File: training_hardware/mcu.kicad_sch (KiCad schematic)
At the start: 2 parts, among them J1 RJ45_LED_Shielded, U1 Teensy4.1_DEV-16771

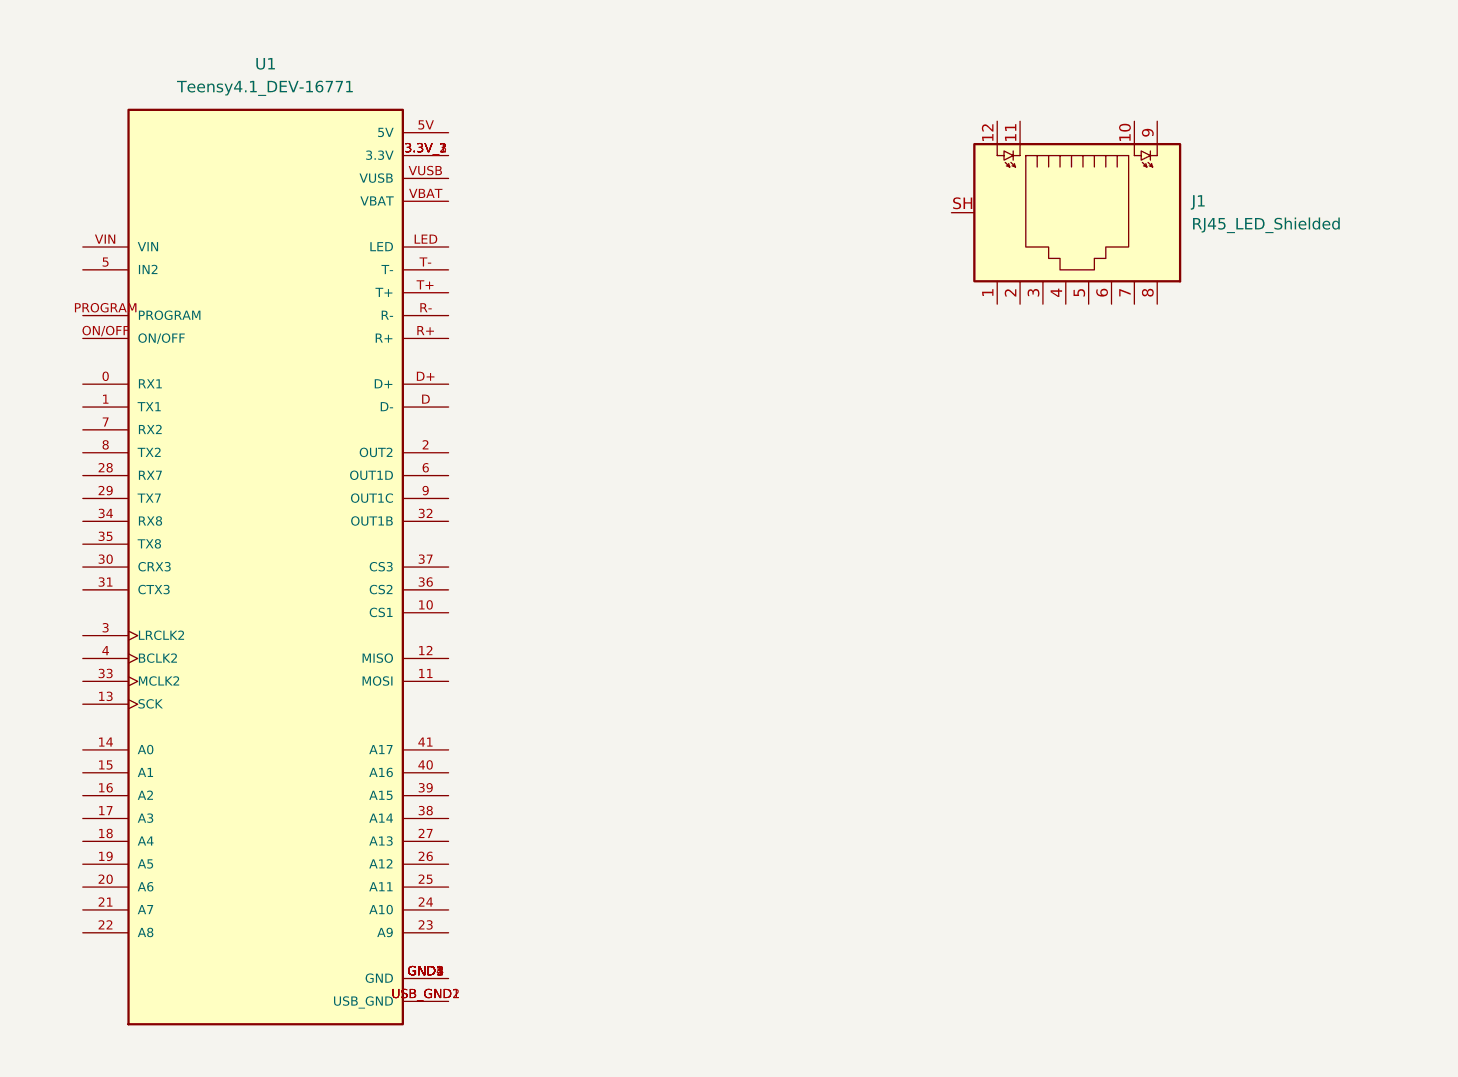
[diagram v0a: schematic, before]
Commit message: Add Ethernet
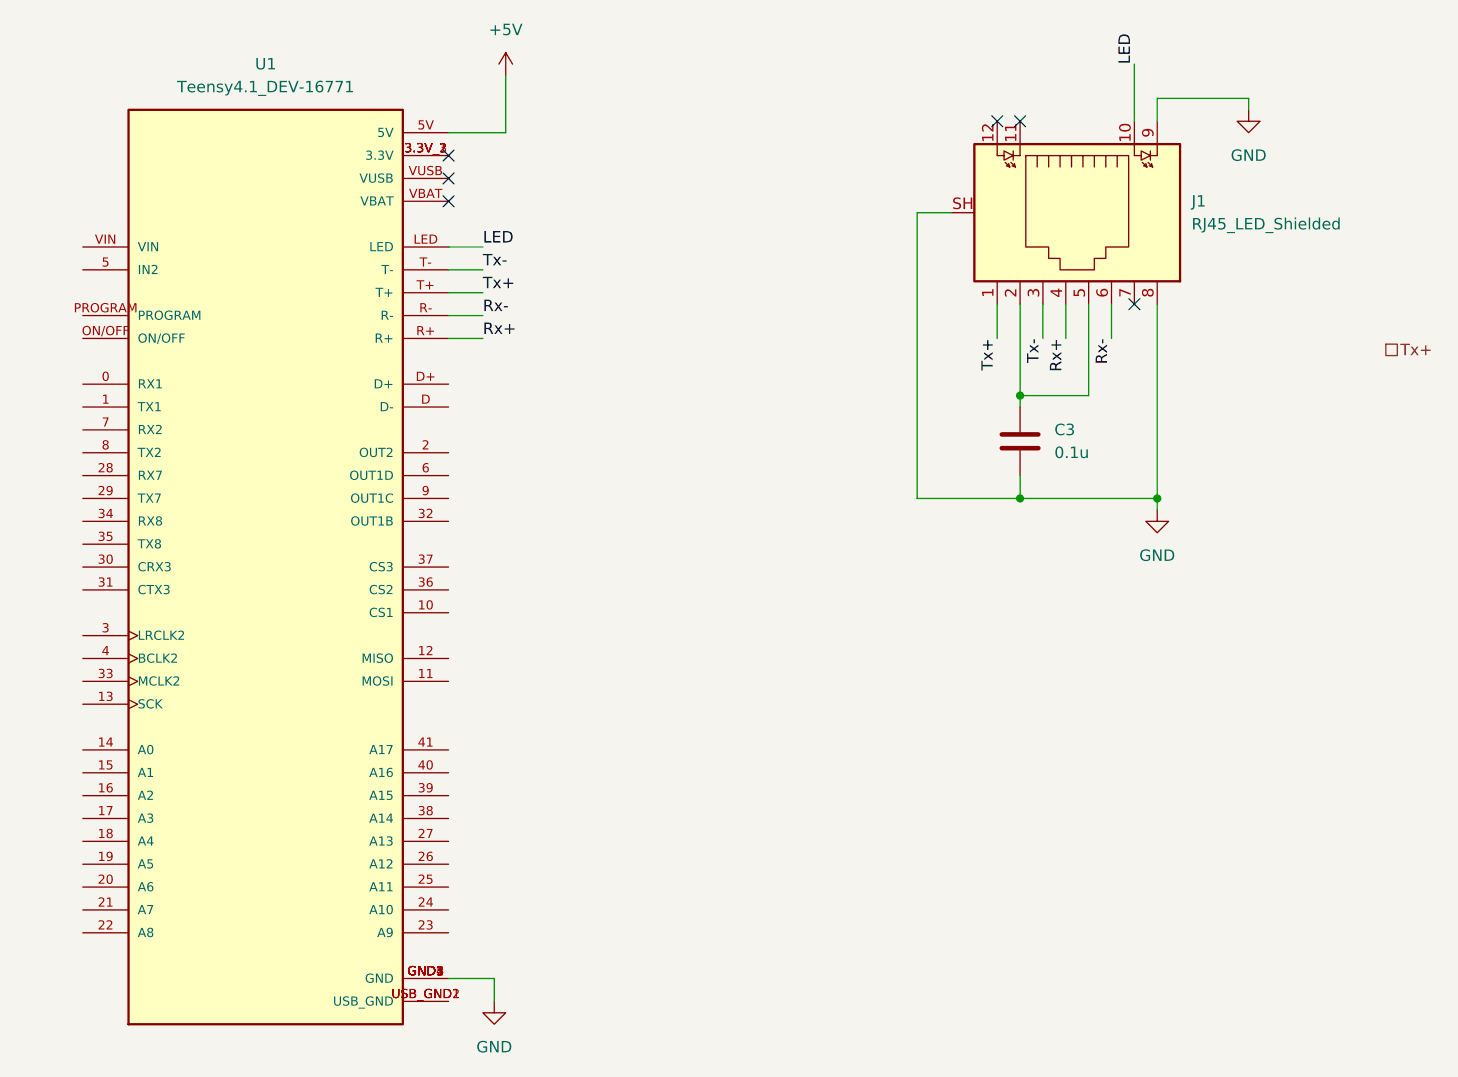
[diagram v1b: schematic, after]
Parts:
- added C3: 0.1u, symbol Device:C
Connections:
- net Tx+: now reaches J1.1
- net Tx+: now also U1.T+
- net LED: now reaches J1.10
- net LED: now also U1.LED
- net at J1.2: now also J1.5, C3.1
- net Tx-: now reaches J1.3
- net Tx-: now also U1.T-
- net Rx+: now reaches J1.4
- net Rx+: now also U1.R+
- net Rx-: now reaches J1.6
- net Rx-: now also U1.R-
- net GND: now reaches J1.8
- net GND: now also J1.9, J1.SH, U1.GND1 (GND), U1.GND2 (GND), U1.GND3 (GND), U1.GND4 (GND), U1.GND5 (GND), C3.2
- net +5V: now reaches U1.5V
- no-connect marks 0 -> 6

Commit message: Finish Schematic
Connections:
- net STBY: now reaches U1.2 (OUT2)
- net CTX1: now reaches U1.22 (A8)
- net CRX1: now reaches U1.23 (A9)
- net +3V3: now reaches U1.3.3V_1 (3.3V), U1.3.3V_2 (3.3V), U1.3.3V_3 (3.3V)
- no-connect marks 6 -> 5
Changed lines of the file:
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@@
-	)
-	(no_connect
-		(at 74.93 54.61)
 	)
 	(no_connect
@@
 	(wire
 		(pts
+			(xy 74.93 54.61) (xy 83.82 54.61)
+		)
+		(stroke
+			(width 0)
+			(type default)
+		)
+	)
+	(wire
+		(pts
 			(xy 127 92.71) (xy 138.43 92.71)
 		)
@@
 	(wire
 		(pts
+			(xy 83.82 45.72) (xy 83.82 54.61)
+		)
+		(stroke
+			(width 0)
+			(type default)
+		)
+	)
+	(wire
+		(pts
 			(xy 74.93 67.31) (xy 78.74 67.31)
 		)
@@
 	(wire
 		(pts
-			(xy 74.93 52.07) (xy 81.28 52.07)
+			(xy 74.93 52.07) (xy 78.74 52.07)
 		)
 		(stroke
@@
 	(wire
 		(pts
-			(xy 81.28 45.72) (xy 81.28 52.07)
+			(xy 78.74 45.72) (xy 78.74 52.07)
 		)
 		(stroke
@@
 			)
 			(justify left bottom)
+		)
+	)
+	(hierarchical_label "STBY"
+		(shape output)
+		(at 74.93 87.63 0)
+		(effects
+			(font
+				(size 1.27 1.27)
+			)
+			(justify left)
+		)
+	)
+	(hierarchical_label "CTX1"
+		(shape output)
+		(at 34.29 140.97 180)
+		(effects
+			(font
+				(size 1.27 1.27)
+			)
+			(justify right)
 		)
 	)
@@
 		(shape passive)
 		(at 179.07 76.2 0)
+		(effects
+			(font
+				(size 1.27 1.27)
+			)
+			(justify left)
+		)
+	)
+	(hierarchical_label "CRX1"
+		(shape input)
+		(at 74.93 140.97 0)
 		(effects
 			(font
@@
 	(symbol
 		(lib_id "power:+5V")
-		(at 81.28 45.72 0)
+		(at 78.74 45.72 0)
 		(unit 1)
 		(exclude_from_sim no)
@@
 		(fields_autoplaced yes)
 		(property "Reference" "#PWR010"
-			(at 81.28 49.53 0)
+			(at 78.74 49.53 0)
 			(effects
 				(font
@@
 		)
 		(property "Value" "+5V"
-			(at 81.28 40.64 0)
+			(at 78.74 40.64 0)
 			(effects
 				(font
@@
 		)
 		(property "Footprint" ""
-			(at 81.28 45.72 0)
+			(at 78.74 45.72 0)
 			(effects
 				(font
@@
 		)
 		(property "Datasheet" ""
-			(at 81.28 45.72 0)
+			(at 78.74 45.72 0)
 			(effects
 				(font
@@
 		)
 		(property "Description" "Power symbol creates a global label with name \"+5V\""
-			(at 81.28 45.72 0)
+			(at 78.74 45.72 0)
 			(effects
 				(font
@@
 					(unit 1)
 				)
+			)
+		)
+	)
+	(symbol
+		(lib_id "power:+3V3")
+		(at 83.82 45.72 0)
+		(unit 1)
+		(exclude_from_sim no)
+		(in_bom yes)
+		(on_board yes)
+		(dnp no)
+		(fields_autoplaced yes)
+		(property "Reference" "#PWR016"
+			(at 83.82 49.53 0)
+			(effects
+				(font
+					(size 1.27 1.27)
+				)
+				(hide yes)
+			)
+		)
+		(property "Value" "+3V3"
+			(at 83.82 40.64 0)
+			(effects
+				(font
+					(size 1.27 1.27)
+				)
+			)
+		)
+		(property "Footprint" ""
+			(at 83.82 45.72 0)
+			(effects
+				(font
+					(size 1.27 1.27)
+				)
+				(hide yes)
+			)
+		)
+		(property "Datasheet" ""
+			(at 83.82 45.72 0)
+			(effects
+				(font
+					(size 1.27 1.27)
+				)
+				(hide yes)
+			)
+		)
+		(property "Description" "Power symbol creates a global label with name \"+3V3\""
+			(at 83.82 45.72 0)
+			(effects
+				(font
+					(size 1.27 1.27)
+				)
+				(hide yes)
+			)
+		)
+		(pin "1"
+		)
+		(instances
+			(project ""
+				(path "/b34dceb0-d8ef-45e4-8aee-3b8caa07fef4/bb915eb3-b9df-433d-8eb5-1ea49d43d74e"
+					(reference "#PWR016")
+					(unit 1)
+				)
